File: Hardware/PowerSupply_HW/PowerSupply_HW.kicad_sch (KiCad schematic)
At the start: 11 parts, among them J10 Debug, J11 Debug, U3 TP4056_MODULE, U4 Modulo_DC-DC_Boost_XL6009

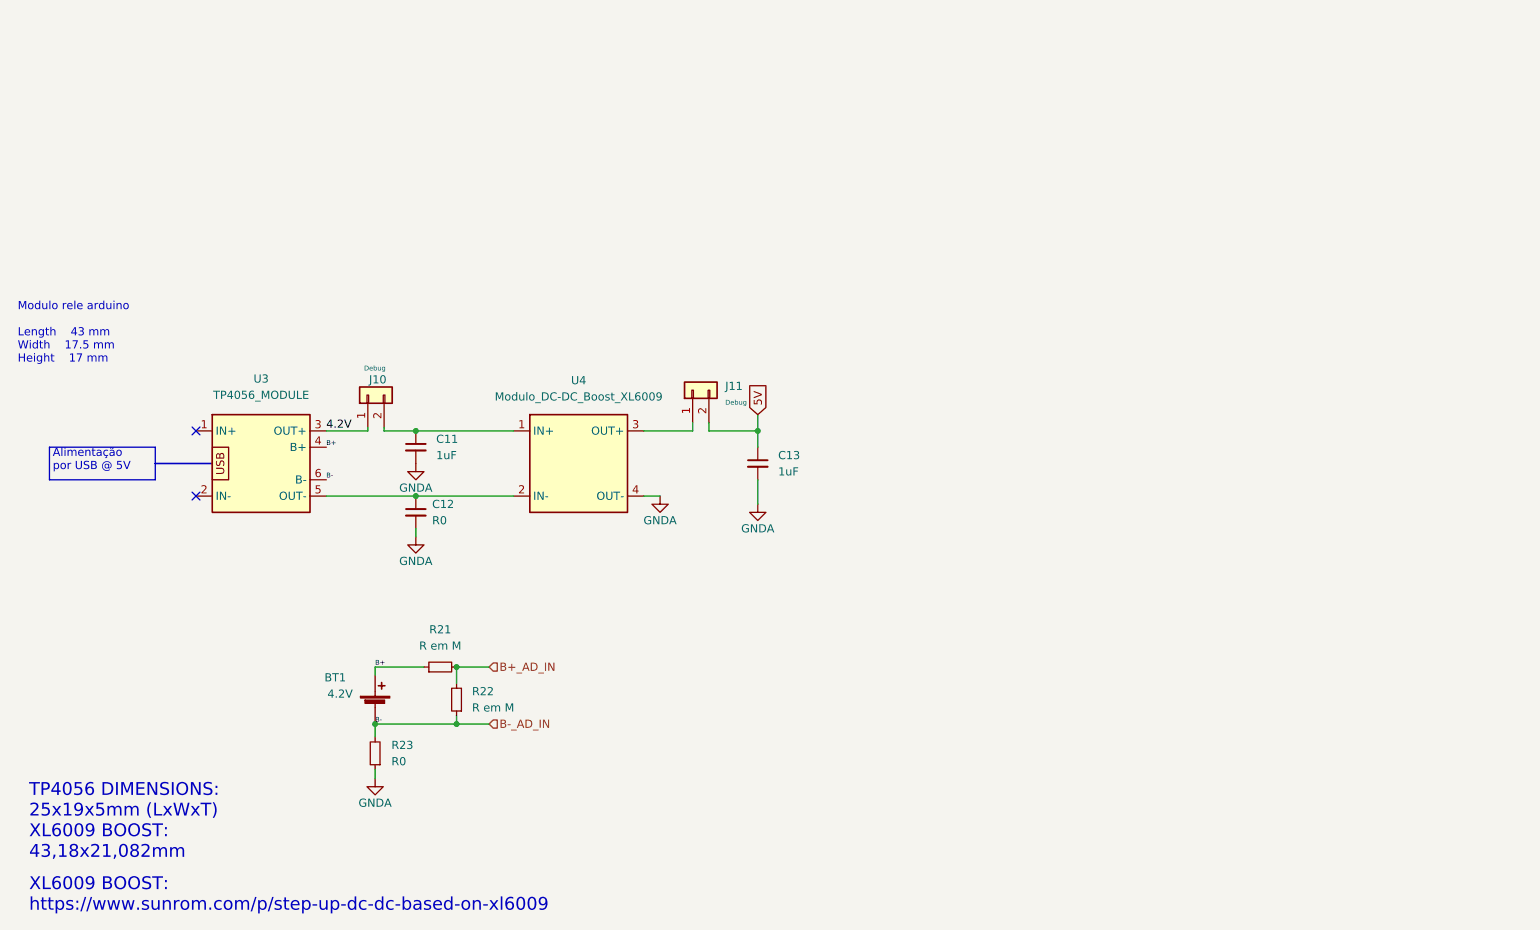
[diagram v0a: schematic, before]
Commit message: Separacao do projeto em 3 PCBs - Core, PowerSupply, Display
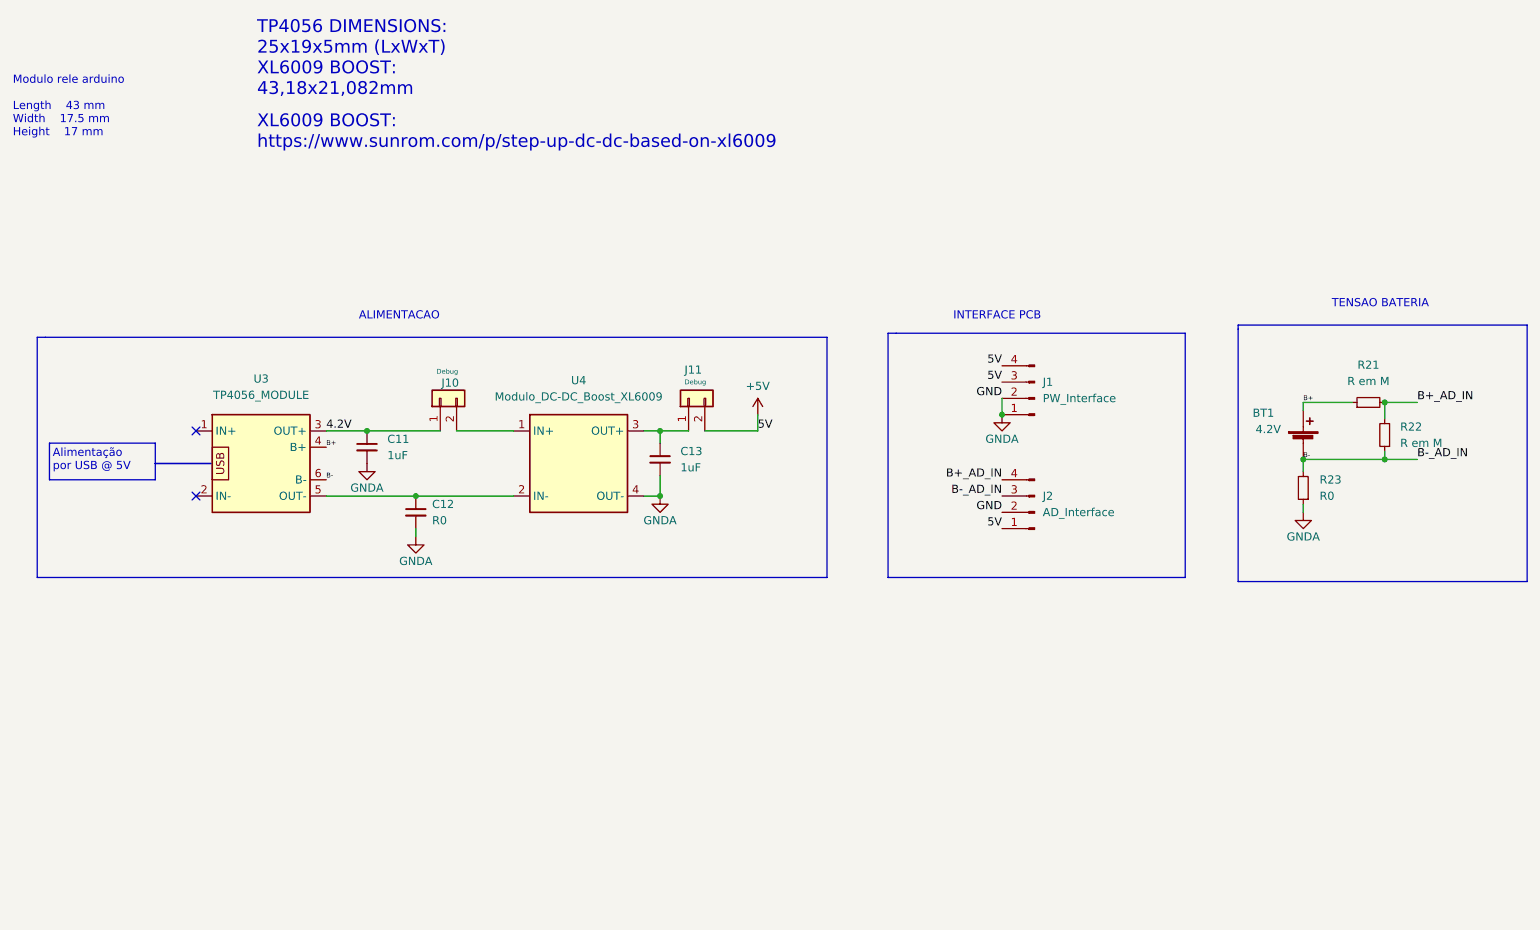
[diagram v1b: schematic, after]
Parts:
- added J1: PW_Interface, Connector_PinHeader_2.54mm:PinHeader_1x04_P2.54mm_Vertical, symbol Connector:Conn_01x04_Male
- added J2: AD_Interface, Connector_PinHeader_2.54mm:PinHeader_1x04_P2.54mm_Vertical, symbol Connector:Conn_01x04_Male
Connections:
- net 4.2V: now also C11.1
- net B+_AD_IN: now also J2.4 (Pin_4)
- net GNDA: now also J1.1 (Pin_1), J1.2 (Pin_2), J2.2 (Pin_2)
- net at J10.2 (Pin_2), U4.1 (IN+): no longer C11.1
- net at J11.1 (Pin_1), U4.3 (OUT+): now also C13.1
- net 5V renamed +5V
- net +5V: now also J1.3 (Pin_3), J1.4 (Pin_4), J2.1 (Pin_1); no longer C13.1
- net B-_AD_IN renamed B-
- net B-: now also J2.3 (Pin_3)
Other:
- note added: "ALIMENTACAO"
- note added: "INTERFACE PCB"
- note added: "TENSAO BATERIA"
- moved on the sheet: BT1, C11, C13, J10, J11, R21, R22, R23

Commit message: geracao de gerbers
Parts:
- added J3: Relay_Interface, Connector_PinHeader_2.54mm:PinHeader_1x04_P2.54mm_Vertical, symbol Connector:Conn_01x04_Male
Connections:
- net +5V: now also J3.3 (Pin_3), J3.4 (Pin_4)
- net GNDA: now also J3.1 (Pin_1), J3.2 (Pin_2)
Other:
- moved on the sheet: J2
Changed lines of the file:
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@@
 (kicad_sch (version 20211123) (generator eeschema)
   (paper "A4")
+  (junction (at 175.895 62.865) (diameter 0) (color 0 0 0 0)
+  )
   (junction (at 123.19 36.83) (diameter 0) (color 0 0 0 0)
   )
@@
   (no_connect (at 50.8 46.99))
   (no_connect (at 50.8 36.83))
-  (polyline (pts (xy 158.75 59.69) (xy 158.75 21.59))
-    (stroke (width 0) (type default) (color 0 0 0 0))
-  )
-  (polyline (pts (xy 205.105 59.69) (xy 158.75 59.69))
-    (stroke (width 0) (type default) (color 0 0 0 0))
-  )
-  (polyline (pts (xy 205.105 21.59) (xy 205.105 59.69))
+  (polyline (pts (xy 158.75 67.945) (xy 158.75 21.59))
+    (stroke (width 0) (type default) (color 0 0 0 0))
+  )
+  (polyline (pts (xy 205.105 67.945) (xy 158.75 67.945))
+    (stroke (width 0) (type default) (color 0 0 0 0))
+  )
+  (polyline (pts (xy 205.105 21.59) (xy 205.105 67.945))
     (stroke (width 0) (type default) (color 0 0 0 0))
   )
@@
   )
   (wire (pts (xy 223.52 32.385) (xy 223.52 33.655))
+    (stroke (width 0) (type default) (color 0 0 0 0))
+  )
+  (wire (pts (xy 175.895 60.325) (xy 175.895 62.865))
     (stroke (width 0) (type default) (color 0 0 0 0))
   )
@@
     (effects (font (size 1.27 1.27)) (justify left bottom))
   )
-  (label "5V" (at 176.53 52.07 180)
+  (label "5V" (at 175.26 50.8 180)
     (effects (font (size 1.27 1.27)) (justify right bottom))
   )
@@
     (effects (font (size 1.27 1.27)) (justify left bottom))
   )
+  (label "5V" (at 175.895 57.785 180)
+    (effects (font (size 1.27 1.27)) (justify right bottom))
+  )
   (label "GND" (at 176.53 31.75 180)
     (effects (font (size 1.27 1.27)) (justify right bottom))
@@
     (effects (font (size 1.27 1.27)) (justify right bottom))
   )
-  (label "B-_AD_IN" (at 176.53 46.99 180)
+  (label "B-_AD_IN" (at 175.26 45.72 180)
+    (effects (font (size 1.27 1.27)) (justify right bottom))
+  )
+  (label "5V" (at 175.895 55.245 180)
     (effects (font (size 1.27 1.27)) (justify right bottom))
   )
@@
     (effects (font (size 0.75 0.75)) (justify left bottom))
   )
-  (label "B+_AD_IN" (at 176.53 44.45 180)
-    (effects (font (size 1.27 1.27)) (justify right bottom))
-  )
-  (label "GND" (at 176.53 49.53 180)
+  (label "B+_AD_IN" (at 175.26 43.18 180)
+    (effects (font (size 1.27 1.27)) (justify right bottom))
+  )
+  (label "GND" (at 175.26 48.26 180)
     (effects (font (size 1.27 1.27)) (justify right bottom))
   )
   (label "5V" (at 138.43 36.83 0)
     (effects (font (size 1.27 1.27)) (justify left bottom))
+  )
+  (label "GND" (at 175.895 60.325 180)
+    (effects (font (size 1.27 1.27)) (justify right bottom))
   )
   (label "B-_AD_IN" (at 241.3 41.275 0)
@@
   (label "B+" (at 223.52 32.385 0)
     (effects (font (size 0.75 0.75)) (justify left bottom))
+  )
+  (symbol (lib_id "power:GNDA") (at 175.895 62.865 0) (unit 1)
+    (in_bom yes) (on_board yes)
+    (property "Reference" "#PWR0103" (id 0) (at 175.895 69.215 0)
+      (effects (font (size 1.27 1.27)) hide)
+    )
+    (property "Value" "GNDA" (id 1) (at 175.895 66.675 0))
+    (property "Footprint" "" (id 2) (at 175.895 62.865 0)
+      (effects (font (size 1.27 1.27)) hide)
+    )
+    (property "Datasheet" "" (id 3) (at 175.895 62.865 0)
+      (effects (font (size 1.27 1.27)) hide)
+    )
+    (pin "1")
   )
   (symbol (lib_id "Connector_Generic:Conn_01x02") (at 88.9 31.75 90) (unit 1)
@@
     (pin "2")
   )
-  (symbol (lib_id "Connector:Conn_01x04_Male") (at 181.61 49.53 180) (unit 1)
-    (in_bom yes) (on_board yes) (fields_autoplaced)
-    (property "Reference" "J2" (id 0) (at 182.88 46.9899 0)
-      (effects (font (size 1.27 1.27)) (justify right))
-    )
-    (property "Value" "AD_Interface" (id 1) (at 182.88 49.5299 0)
-      (effects (font (size 1.27 1.27)) (justify right))
-    )
-    (property "Footprint" "Connector_PinHeader_2.54mm:PinHeader_1x04_P2.54mm_Vertical" (id 2) (at 181.61 49.53 0)
-      (effects (font (size 1.27 1.27)) hide)
-    )
-    (property "Datasheet" "~" (id 3) (at 181.61 49.53 0)
+  (symbol (lib_id "Connector:Conn_01x04_Male") (at 180.34 48.26 180) (unit 1)
+    (in_bom yes) (on_board yes) (fields_autoplaced)
+    (property "Reference" "J2" (id 0) (at 181.61 45.7199 0)
+      (effects (font (size 1.27 1.27)) (justify right))
+    )
+    (property "Value" "AD_Interface" (id 1) (at 181.61 48.2599 0)
+      (effects (font (size 1.27 1.27)) (justify right))
+    )
+    (property "Footprint" "Connector_PinHeader_2.54mm:PinHeader_1x04_P2.54mm_Vertical" (id 2) (at 180.34 48.26 0)
+      (effects (font (size 1.27 1.27)) hide)
+    )
+    (property "Datasheet" "~" (id 3) (at 180.34 48.26 0)
       (effects (font (size 1.27 1.27)) hide)
     )
@@
     (pin "2")
   )
+  (symbol (lib_id "Connector:Conn_01x04_Male") (at 180.975 60.325 180) (unit 1)
+    (in_bom yes) (on_board yes) (fields_autoplaced)
+    (property "Reference" "J3" (id 0) (at 182.88 57.7849 0)
+      (effects (font (size 1.27 1.27)) (justify right))
+    )
+    (property "Value" "Relay_Interface" (id 1) (at 182.88 60.3249 0)
+      (effects (font (size 1.27 1.27)) (justify right))
+    )
+    (property "Footprint" "Connector_PinHeader_2.54mm:PinHeader_1x04_P2.54mm_Vertical" (id 2) (at 180.975 60.325 0)
+      (effects (font (size 1.27 1.27)) hide)
+    )
+    (property "Datasheet" "~" (id 3) (at 180.975 60.325 0)
+      (effects (font (size 1.27 1.27)) hide)
+    )
+    (pin "1")
+    (pin "2")
+    (pin "3")
+    (pin "4")
+  )
   (symbol (lib_id "Device:C_Small") (at 85.09 49.53 0) (unit 1)
     (in_bom yes) (on_board yes) (fields_autoplaced)
@@
       (reference "#PWR0102") (unit 1) (value "+5V") (footprint "")
     )
+    (path "/151c2306-b0cb-4a7c-964d-e0dbe981c39a"
+      (reference "#PWR0103") (unit 1) (value "GNDA") (footprint "")
+    )
     (path "/ce8520ef-3686-4681-8701-68d342405a8d"
       (reference "#PWR0117") (unit 1) (value "GNDA") (footprint "")
@@
       (reference "J2") (unit 1) (value "AD_Interface") (footprint "Connector_PinHeader_2.54mm:PinHeader_1x04_P2.54mm_Vertical")
     )
+    (path "/9954cffd-fe94-4452-9be6-a9bdcb43cc84"
+      (reference "J3") (unit 1) (value "Relay_Interface") (footprint "Connector_PinHeader_2.54mm:PinHeader_1x04_P2.54mm_Vertical")
+    )
     (path "/229584ac-4825-4f5a-b5d6-fc600b7d6c9b"
